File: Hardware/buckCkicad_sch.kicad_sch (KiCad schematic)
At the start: 18 parts, among them U6 SiC437BED-T1-GE3

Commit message: updated sensors and other stuff
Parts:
- R31: value 200k -> 499k
- U6: value SiC437BED-T1-GE3 -> SiC438BED-T1-GE3
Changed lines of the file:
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@@
 		)
 	)
+	(wire
+		(pts
+			(xy 62.992 60.96) (xy 62.992 58.42)
+		)
+		(stroke
+			(width 0)
+			(type default)
+		)
+	)
 	(polyline
 		(pts
@@
 	(wire
 		(pts
+			(xy 60.96 56.388) (xy 60.96 55.88)
+		)
+		(stroke
+			(width 0)
+			(type default)
+		)
+	)
+	(wire
+		(pts
 			(xy 110.49 53.34) (xy 120.65 53.34)
 		)
@@
 		)
 	)
+	(wire
+		(pts
+			(xy 60.96 55.88) (xy 74.93 55.88)
+		)
+		(stroke
+			(width 0)
+			(type default)
+		)
+	)
 	(polyline
 		(pts
@@
 	(wire
 		(pts
-			(xy 62.23 55.88) (xy 74.93 55.88)
+			(xy 120.65 49.53) (xy 124.46 49.53)
 		)
 		(stroke
@@
 	(wire
 		(pts
-			(xy 120.65 49.53) (xy 124.46 49.53)
+			(xy 140.97 60.96) (xy 142.24 60.96)
 		)
 		(stroke
@@
 	(wire
 		(pts
-			(xy 140.97 60.96) (xy 142.24 60.96)
+			(xy 74.93 63.5) (xy 74.93 66.04)
 		)
 		(stroke
@@
 	(wire
 		(pts
-			(xy 74.93 63.5) (xy 74.93 66.04)
+			(xy 58.42 86.36) (xy 57.15 86.36)
 		)
 		(stroke
@@
 	(wire
 		(pts
-			(xy 58.42 86.36) (xy 57.15 86.36)
+			(xy 140.97 111.76) (xy 146.05 111.76)
 		)
 		(stroke
@@
 	(wire
 		(pts
-			(xy 140.97 111.76) (xy 146.05 111.76)
+			(xy 113.792 50.8) (xy 110.49 50.8)
 		)
 		(stroke
@@
 	(wire
 		(pts
-			(xy 62.23 58.42) (xy 74.93 58.42)
+			(xy 62.992 58.42) (xy 74.93 58.42)
 		)
 		(stroke
@@
 	(symbol
 		(lib_id "power:GND")
-		(at 62.23 58.42 270)
+		(at 62.992 60.96 0)
 		(unit 1)
 		(exclude_from_sim no)
@@
 		(dnp no)
 		(property "Reference" "#PWR061"
-			(at 55.88 58.42 0)
+			(at 62.992 67.31 0)
 			(effects
 				(font
@@
 		)
 		(property "Value" "GND"
-			(at 54.61 58.42 90)
+			(at 62.992 68.58 90)
 			(effects
 				(font
@@
 				)
 				(justify left)
+				(hide yes)
 			)
 		)
 		(property "Footprint" ""
-			(at 62.23 58.42 0)
+			(at 62.992 60.96 0)
 			(effects
 				(font
@@
 		)
 		(property "Datasheet" ""
-			(at 62.23 58.42 0)
+			(at 62.992 60.96 0)
 			(effects
 				(font
@@
 		)
 		(property "Description" ""
-			(at 62.23 58.42 0)
+			(at 62.992 60.96 0)
 			(effects
 				(font
@@
 	(symbol
 		(lib_id "power:GNDA")
-		(at 110.49 50.8 90)
+		(at 113.792 50.8 0)
 		(unit 1)
 		(exclude_from_sim no)
@@
 		(on_board yes)
 		(dnp no)
-		(fields_autoplaced yes)
 		(property "Reference" "#PWR068"
-			(at 116.84 50.8 0)
+			(at 113.792 57.15 0)
 			(effects
 				(font
@@
 		)
 		(property "Value" "GNDA"
-			(at 113.665 51.2338 90)
+			(at 116.84 50.8 0)
 			(effects
 				(font
 					(size 1.27 1.27)
 				)
-				(justify right)
 			)
 		)
 		(property "Footprint" ""
-			(at 110.49 50.8 0)
+			(at 113.792 50.8 0)
 			(effects
 				(font
@@
 		)
 		(property "Datasheet" ""
-			(at 110.49 50.8 0)
+			(at 113.792 50.8 0)
 			(effects
 				(font
@@
 		)
 		(property "Description" ""
-			(at 110.49 50.8 0)
+			(at 113.792 50.8 0)
 			(effects
 				(font
@@
 			)
 		)
-		(property "Value" "SiC437BED-T1-GE3"
+		(property "Value" "SiC438BED-T1-GE3"
 			(at 92.71 45.72 0)
 			(effects
@@
 		(dnp no)
 		(property "Reference" "R25"
-			(at 60.96 82.55 90)
+			(at 64.77 82.55 90)
 			(effects
 				(font
@@
 	(symbol
 		(lib_id "power:GND")
-		(at 62.23 55.88 270)
+		(at 60.96 56.388 0)
 		(unit 1)
 		(exclude_from_sim no)
@@
 		(dnp no)
 		(property "Reference" "#PWR060"
-			(at 55.88 55.88 0)
+			(at 60.96 62.738 0)
 			(effects
 				(font
@@
 		)
 		(property "Value" "GND"
-			(at 54.61 55.88 90)
+			(at 60.96 64.008 90)
 			(effects
 				(font
@@
 				)
 				(justify left)
+				(hide yes)
 			)
 		)
 		(property "Footprint" ""
-			(at 62.23 55.88 0)
+			(at 60.96 56.388 0)
 			(effects
 				(font
@@
 		)
 		(property "Datasheet" ""
-			(at 62.23 55.88 0)
+			(at 60.96 56.388 0)
 			(effects
 				(font
@@
 		)
 		(property "Description" ""
-			(at 62.23 55.88 0)
+			(at 60.96 56.388 0)
 			(effects
 				(font
@@
 			)
 		)
-		(property "Value" "200k"
+		(property "Value" "499k"
 			(at 138.43 58.4169 90)
 			(effects

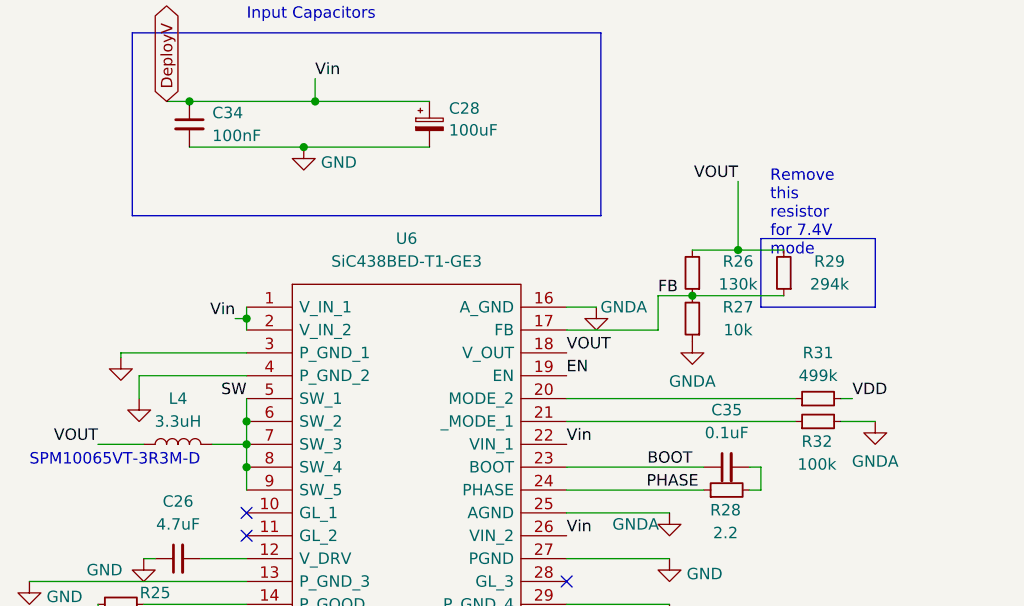
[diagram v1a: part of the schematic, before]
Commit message: Finished Boosts and Sensors
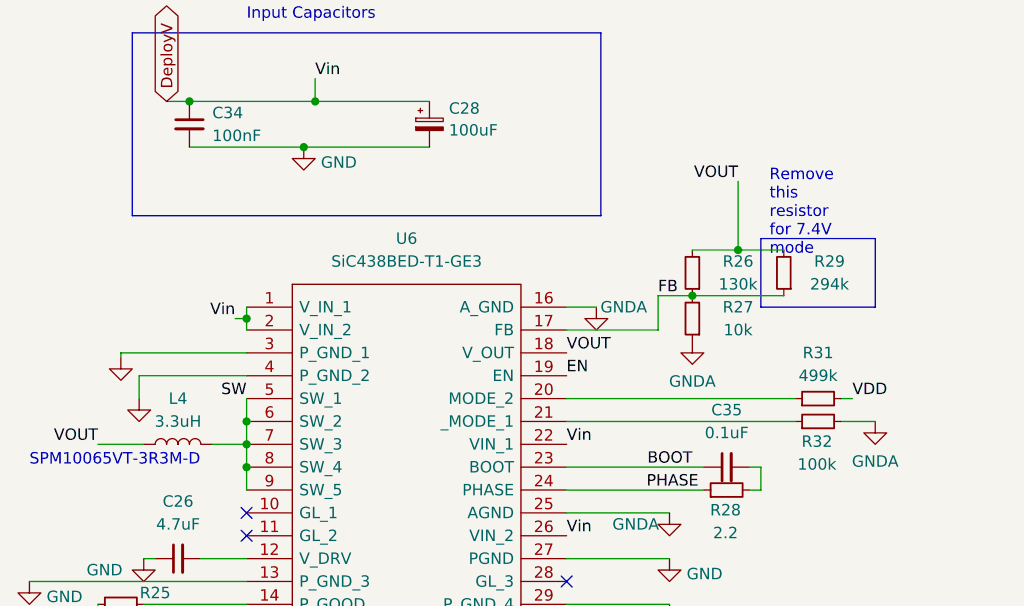
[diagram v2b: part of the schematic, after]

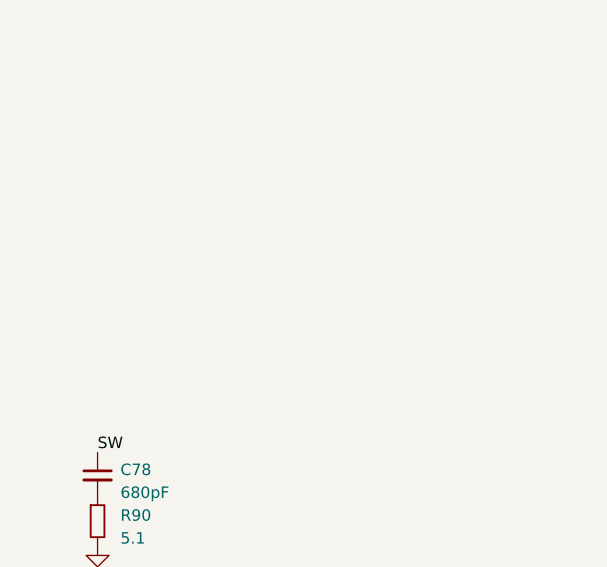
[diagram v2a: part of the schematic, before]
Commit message: Added actuators and I2C bus
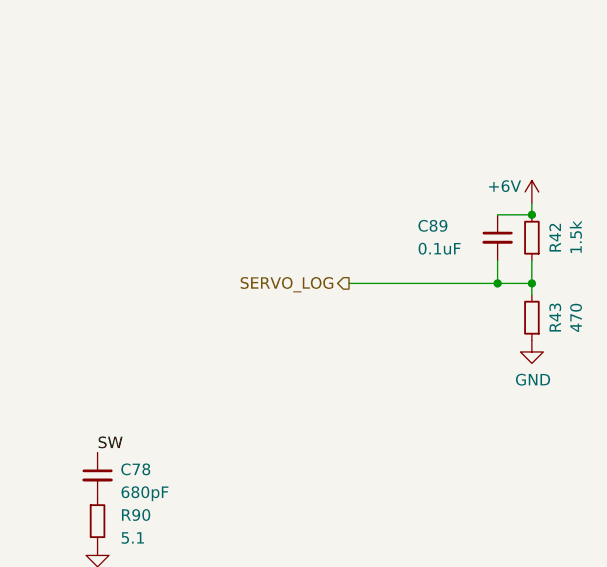
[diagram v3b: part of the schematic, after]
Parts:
- added C89: 0.1uF, Capacitor_SMD:C_0402_1005Metric, symbol Device:C_Small
- added R42: 1.5k, Resistor_SMD:R_0402_1005Metric, symbol Device:R_Small
- added R43: 470, Resistor_SMD:R_0402_1005Metric, symbol Device:R_Small
- C28: footprint Capacitor_Tantalum_SMD:CP_EIA-7343-40_Kemet-Y -> Capacitor_Tantalum_SMD:CP_EIA-7360-38_Kemet-E
- L4: footprint Inductor_SMD:ETQP5M6M_YLC -> iclr:IND_SPM10065VT-3R3M-D
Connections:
- net +6V: now also C89.1, R42.2
- net GND: now also R43.1
- new net SERVO_LOG: C89.2, R42.1, R43.2

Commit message: v2 Ready for Review
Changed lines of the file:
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@@
 	(polyline
 		(pts
-			(xy 62.23 20.32) (xy 64.77 20.32)
+			(xy 55.49 20.35) (xy 64.77 20.35)
 		)
 		(stroke
@@
 	(polyline
 		(pts
-			(xy 62.23 40.64) (xy 62.23 20.32)
+			(xy 55.49 40.67) (xy 55.49 20.35)
 		)
 		(stroke
@@
 	(polyline
 		(pts
-			(xy 114.3 40.64) (xy 62.23 40.64)
+			(xy 114.3 40.67) (xy 55.49 40.67)
 		)
 		(stroke
@@
 	(global_label "DeployV"
 		(shape bidirectional)
-		(at 66.04 27.94 90)
+		(at 66.04 27.94 180)
 		(fields_autoplaced yes)
 		(effects
@@
 				(size 1.27 1.27)
 			)
-			(justify left)
+			(justify right)
 		)
 		(property "Intersheetrefs" "${INTERSHEET_REFS}"
-			(at 66.04 17.2785 90)
+			(at 55.3785 27.94 0)
 			(effects
 				(font
 					(size 1.27 1.27)
 				)
-				(justify left)
+				(justify right)
 				(hide yes)
 			)

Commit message: Most Review Changes
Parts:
- C78: value 680pF -> 160pF
- U6: value SiC438BED-T1-GE3 -> SiC437BED-T1-GE3
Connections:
- net +6V: no longer C89.1
- net GND: now also C89.2
- net SERVO_LOG: now also C89.1; no longer C89.2
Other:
- moved on the sheet: C89
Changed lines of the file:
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@@
 	)
 	(junction
-		(at 211.582 39.116)
-		(diameter 0)
-		(color 0 0 0 0)
-	)
-	(junction
 		(at 74.93 52.07)
 		(diameter 0)
@@
 	)
 	(junction
+		(at 211.582 54.102)
+		(diameter 0)
+		(color 0 0 0 0)
+	)
+	(junction
 		(at 68.58 27.94)
 		(diameter 0)
@@
 	(wire
 		(pts
+			(xy 211.582 54.102) (xy 211.582 53.086)
+		)
+		(stroke
+			(width 0)
+			(type default)
+		)
+	)
+	(wire
+		(pts
 			(xy 58.42 86.36) (xy 74.93 86.36)
 		)
@@
 	(wire
 		(pts
+			(xy 211.582 54.864) (xy 211.582 54.102)
+		)
+		(stroke
+			(width 0)
+			(type default)
+		)
+	)
+	(wire
+		(pts
 			(xy 211.582 44.196) (xy 211.582 46.736)
 		)
@@
 	(wire
 		(pts
+			(xy 207.772 46.736) (xy 207.772 48.006)
+		)
+		(stroke
+			(width 0)
+			(type default)
+		)
+	)
+	(wire
+		(pts
 			(xy 146.05 104.14) (xy 146.05 102.87)
 		)
@@
 	(wire
 		(pts
+			(xy 207.772 53.086) (xy 207.772 54.102)
+		)
+		(stroke
+			(width 0)
+			(type default)
+		)
+	)
+	(wire
+		(pts
 			(xy 68.58 33.02) (xy 81.28 33.02)
 		)
@@
 	(wire
 		(pts
+			(xy 207.772 54.102) (xy 211.582 54.102)
+		)
+		(stroke
+			(width 0)
+			(type default)
+		)
+	)
+	(wire
+		(pts
 			(xy 121.92 83.82) (xy 110.49 83.82)
 		)
@@
 	(wire
 		(pts
-			(xy 207.772 39.116) (xy 211.582 39.116)
-		)
-		(stroke
-			(width 0)
-			(type default)
-		)
-	)
-	(wire
-		(pts
 			(xy 58.42 86.36) (xy 57.15 86.36)
 		)
@@
 	(wire
 		(pts
-			(xy 207.772 44.196) (xy 207.772 46.736)
-		)
-		(stroke
-			(width 0)
-			(type default)
-		)
-	)
-	(wire
-		(pts
 			(xy 68.58 27.94) (xy 82.55 27.94)
 		)
@@
 		(fields_autoplaced yes)
 		(property "Reference" "C78"
-			(at 165.862 67.4433 0)
+			(at 166.37 66.8082 0)
 			(effects
 				(font
@@
 			)
 		)
-		(property "Value" "680pF"
-			(at 165.862 69.9833 0)
+		(property "Value" "160pF"
+			(at 166.37 69.3482 0)
 			(effects
 				(font
@@
 			)
 		)
-		(property "Value" "SiC438BED-T1-GE3"
+		(property "Value" "SiC437BED-T1-GE3"
 			(at 92.71 45.72 0)
 			(effects
@@
 	(symbol
 		(lib_id "power:GND")
-		(at 211.582 53.086 0)
+		(at 211.582 54.864 0)
 		(unit 1)
 		(exclude_from_sim no)
@@
 		(dnp no)
 		(property "Reference" "#PWR0177"
-			(at 211.582 59.436 0)
+			(at 211.582 61.214 0)
 			(effects
 				(font
@@
 		)
 		(property "Value" "GND"
-			(at 211.709 57.4802 0)
+			(at 211.709 59.2582 0)
 			(effects
 				(font
@@
 		)
 		(property "Footprint" ""
-			(at 211.582 53.086 0)
+			(at 211.582 54.864 0)
 			(effects
 				(font
@@
 		)
 		(property "Datasheet" ""
-			(at 211.582 53.086 0)
+			(at 211.582 54.864 0)
 			(effects
 				(font
@@
 		)
 		(property "Description" ""
-			(at 211.582 53.086 0)
+			(at 211.582 54.864 0)
 			(effects
 				(font
@@
 	(symbol
 		(lib_id "Device:C_Small")
-		(at 207.772 41.656 0)
+		(at 207.772 50.546 0)
 		(unit 1)
 		(exclude_from_sim no)
@@
 		(dnp no)
 		(property "Reference" "C89"
-			(at 198.882 40.386 0)
+			(at 198.882 49.276 0)
 			(effects
 				(font
@@
 		)
 		(property "Value" "0.1uF"
-			(at 198.882 42.926 0)
+			(at 198.882 51.816 0)
 			(effects
 				(font
@@
 		)
 		(property "Footprint" "Capacitor_SMD:C_0402_1005Metric"
-			(at 207.772 41.656 0)
+			(at 207.772 50.546 0)
 			(effects
 				(font
@@
 		)
 		(property "Datasheet" "~"
-			(at 207.772 41.656 0)
+			(at 207.772 50.546 0)
 			(effects
 				(font
@@
 		)
 		(property "Description" ""
-			(at 207.772 41.656 0)
+			(at 207.772 50.546 0)
 			(effects
 				(font

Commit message: Solenoid Feature and minor changes
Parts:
- R29: footprint Resistor_SMD:R_0402_1005Metric -> Resistor_SMD:R_0603_1608Metric_Pad0.98x0.95mm_HandSolder
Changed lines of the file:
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@@
 			)
 		)
-		(property "Footprint" "Resistor_SMD:R_0402_1005Metric"
+		(property "Footprint" "Resistor_SMD:R_0603_1608Metric_Pad0.98x0.95mm_HandSolder"
 			(at 134.62 46.99 0)
 			(effects

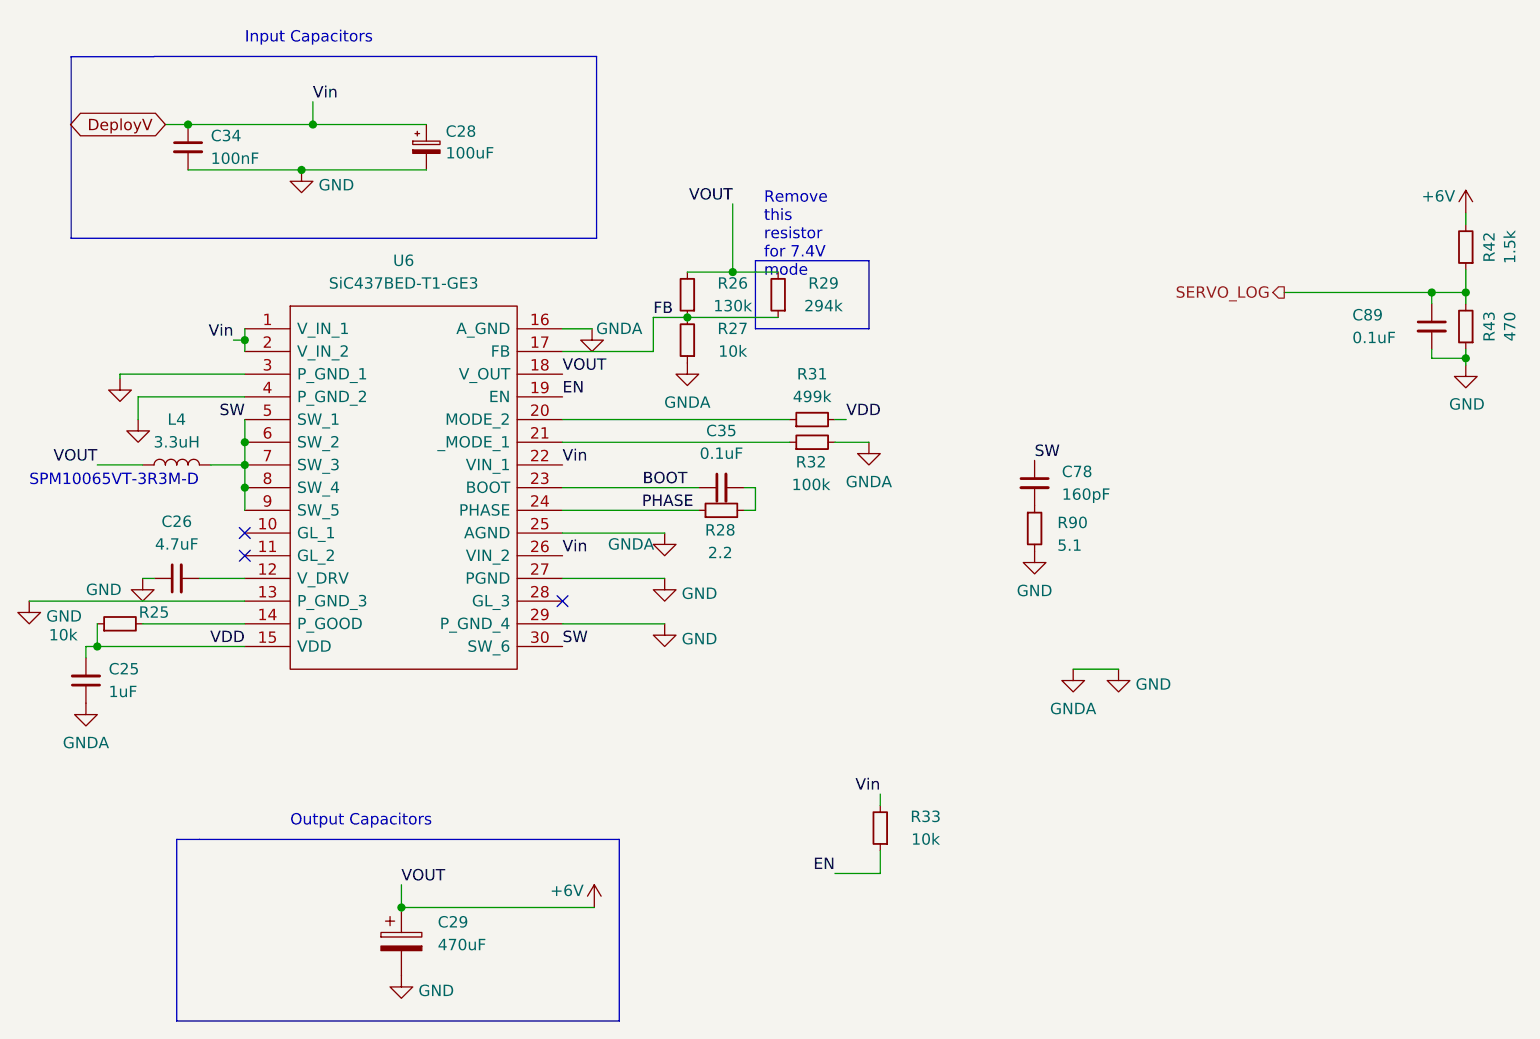
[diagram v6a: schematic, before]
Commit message: schematic reformatting and bom consolidation
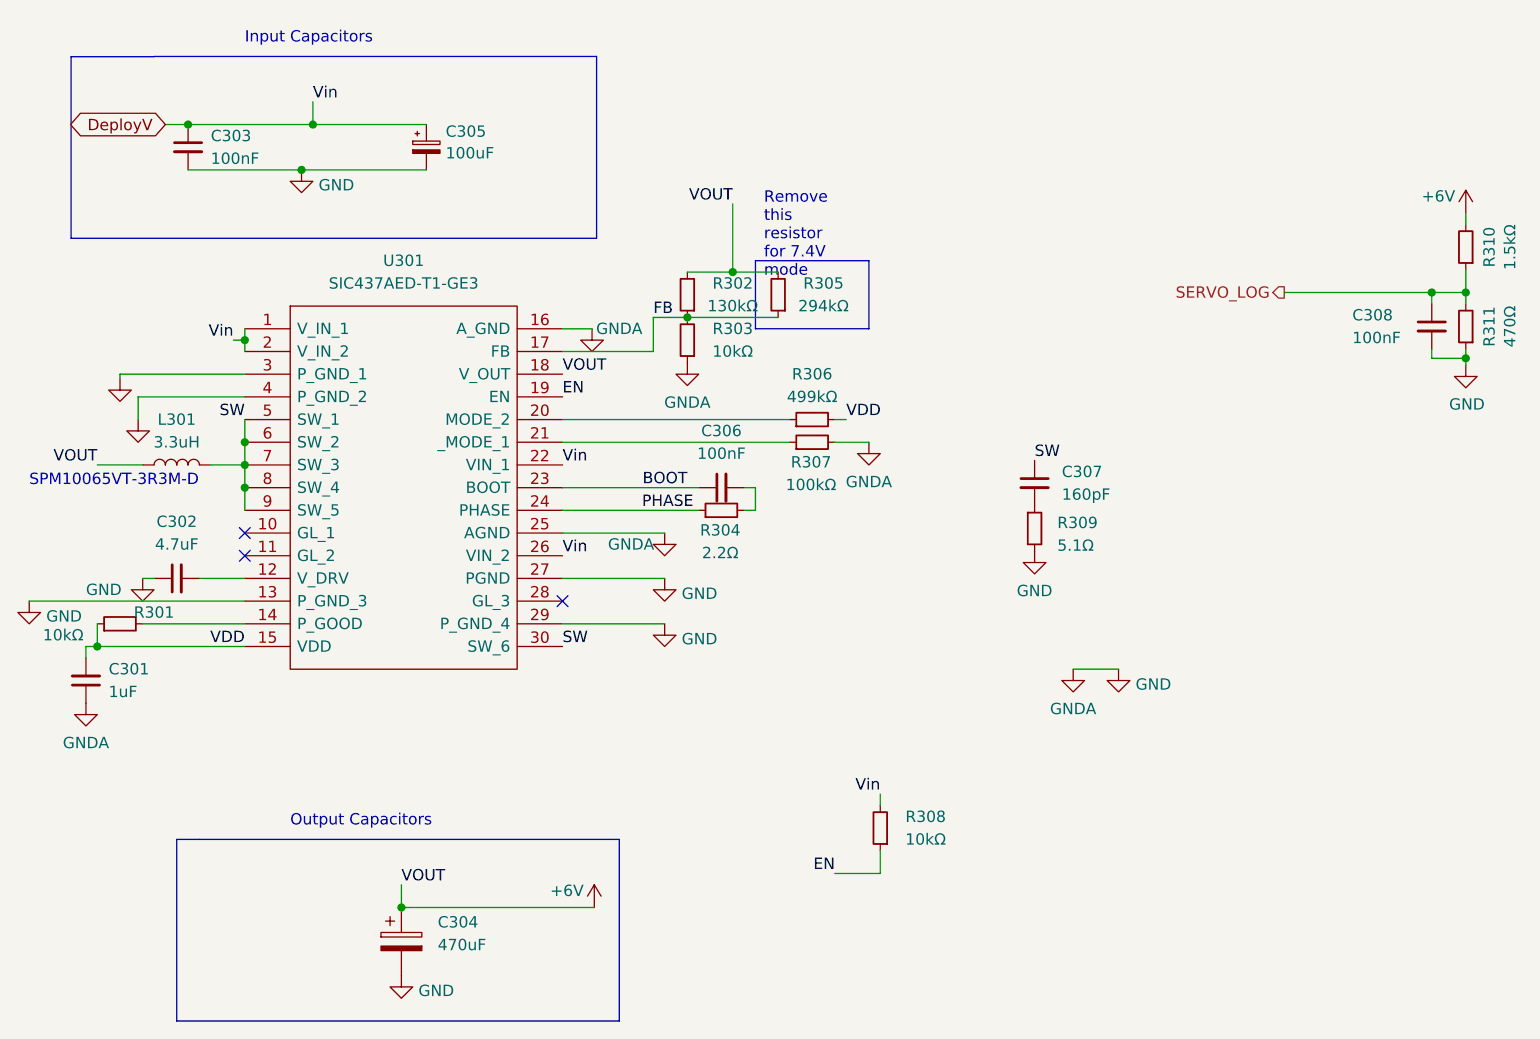
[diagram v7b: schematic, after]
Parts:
- C306: renamed from C35; value 0.1uF -> 100nF
- C308: renamed from C89; value 0.1uF -> 100nF
- R301: renamed from R25; value 10k -> 10kΩ
- R302: renamed from R26; value 130k -> 130kΩ
- R303: renamed from R27; value 10k -> 10kΩ
- R304: renamed from R28; value 2.2 -> 2.2Ω
- R305: renamed from R29; value 294k -> 294kΩ
- R306: renamed from R31; value 499k -> 499kΩ
- R307: renamed from R32; value 100k -> 100kΩ
- R308: renamed from R33; value 10k -> 10kΩ
- R309: renamed from R90; value 5.1 -> 5.1Ω
- R310: renamed from R42; value 1.5k -> 1.5kΩ
- R311: renamed from R43; value 470 -> 470Ω
- U301: renamed from U6; value SiC437BED-T1-GE3 -> SIC437AED-T1-GE3
- renumbered C25 to C301, C26 to C302, C34 to C303, C29 to C304, C28 to C305, C78 to C307, L4 to L301
